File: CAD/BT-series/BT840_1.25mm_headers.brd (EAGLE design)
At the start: 33.4 x 25.1 mm, 64 parts, among them J1 SM02B-SRSS-TB(LF)(SN), U1 TPD4S012DRYR, U2 BT840, U3 LP5907MFX-3.3/NOPB, U4 LP5907MFX-3.3/NOPB, U5 ADS131M08IPBS, U6 BQ24072RGTR, U7 DX4R005JJ2R1800, X1 ABM3B-8.000MHZ-B2-T, X2 FC-12M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

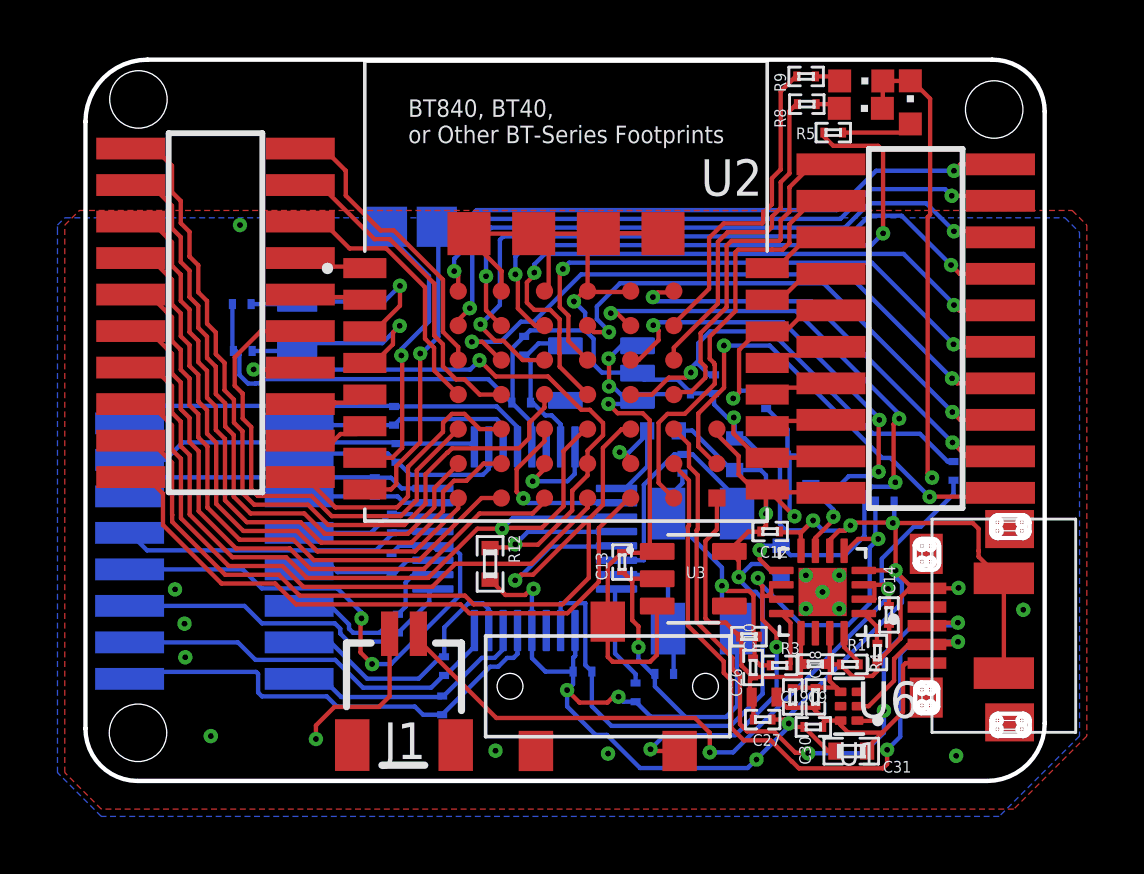
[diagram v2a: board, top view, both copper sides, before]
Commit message: add cam outputs for bt series with some corrections
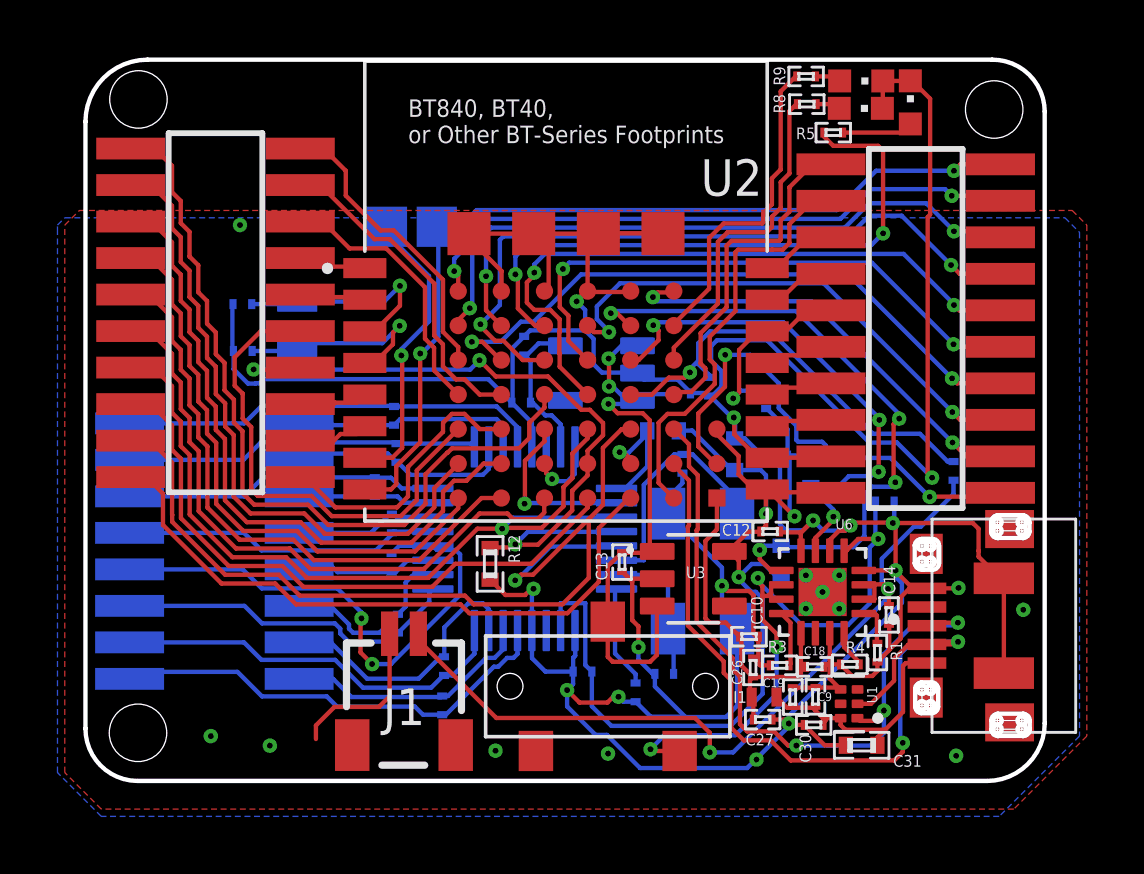
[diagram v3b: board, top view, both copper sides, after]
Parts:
- moved C31 0.42 mm to (34.3, 43.1)
- moved R7 0.20 mm to (29.0, 55.6)
- moved C18 0.10 mm to (32.7, 45.8)
- moved U1 0.08 mm to (33.9, 44.6)
- moved C30 0.07 mm to (32.7, 43.8)
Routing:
- net GND: track 164.8 -> 176.7 mm, vias 25 -> 22
- net SYNC/RESET: track 3.30 -> 2.55 mm
- net DCCH: track 16.6 -> 17.1 mm
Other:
- board text added: "I1"
